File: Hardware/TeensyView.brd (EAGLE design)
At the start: 35.6 x 17.8 mm, 23 parts, among them J1 DNP, J2 DNP

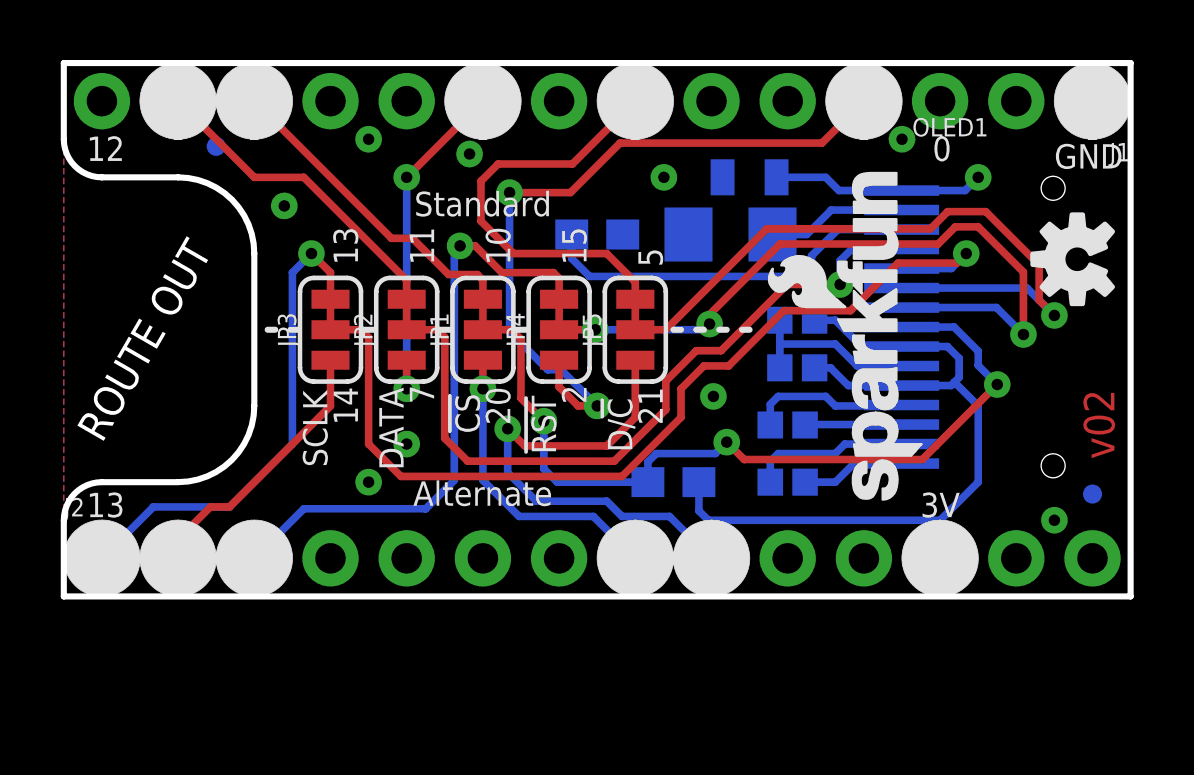
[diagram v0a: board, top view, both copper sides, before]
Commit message: Adjusted proto 2 in prep for reds review
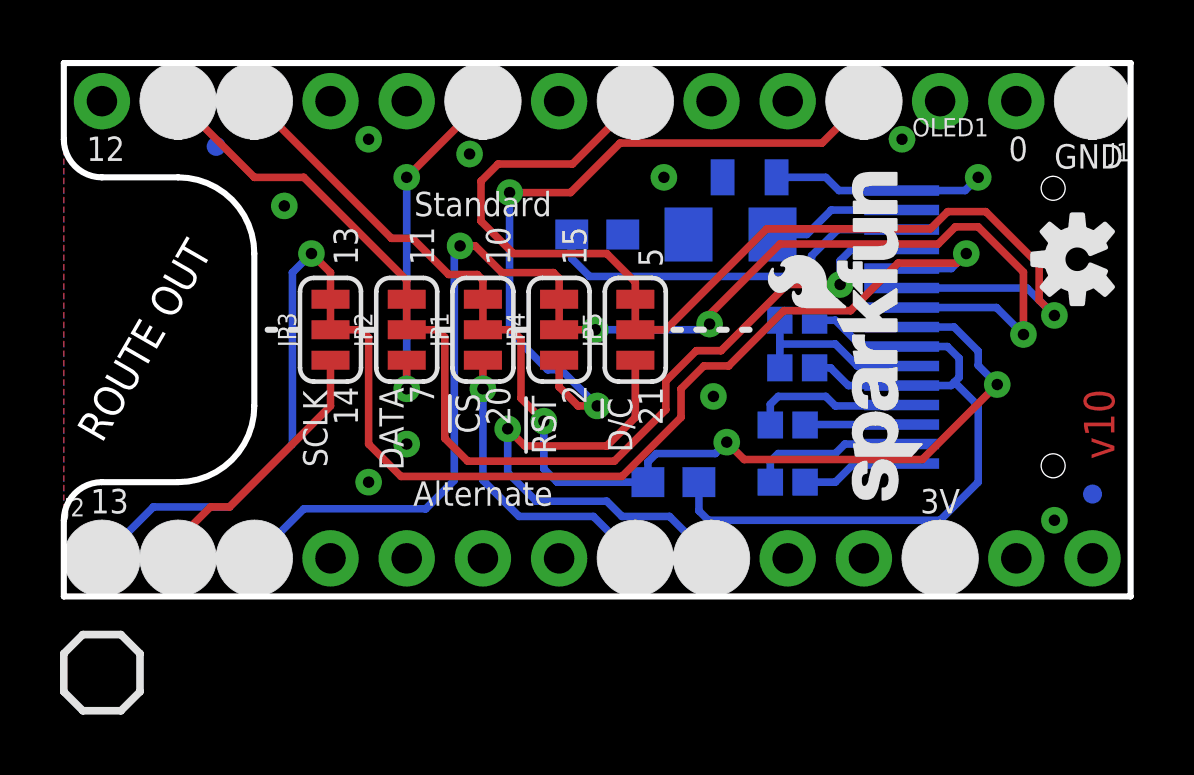
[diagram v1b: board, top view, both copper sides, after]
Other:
- board text added: "v10"
- board text removed: "v02"
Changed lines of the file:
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@@
 <?xml version="1.0" encoding="utf-8"?>
 <!DOCTYPE eagle SYSTEM "eagle.dtd">
-<eagle version="7.5.0">
+<eagle version="7.7.0">
 <drawing>
 <settings>
@@
 <setting verticaltext="up"/>
 </settings>
-<grid distance="0.05" unitdist="inch" unit="inch" style="lines" multiple="1" display="yes" altdistance="0.005" altunitdist="inch" altunit="inch"/>
+<grid distance="0.05" unitdist="inch" unit="inch" style="lines" multiple="1" display="yes" altdistance="0.0025" altunitdist="inch" altunit="inch"/>
 <layers>
-<layer number="1" name="Top" color="4" fill="1" visible="no" active="yes"/>
+<layer number="1" name="Top" color="4" fill="1" visible="yes" active="yes"/>
 <layer number="2" name="Route2" color="1" fill="3" visible="no" active="no"/>
 <layer number="3" name="Route3" color="4" fill="3" visible="no" active="no"/>
@@
 <layer number="19" name="Unrouted" color="6" fill="1" visible="yes" active="yes"/>
 <layer number="20" name="Dimension" color="15" fill="1" visible="yes" active="yes"/>
-<layer number="21" name="tPlace" color="16" fill="1" visible="no" active="yes"/>
+<layer number="21" name="tPlace" color="16" fill="1" visible="yes" active="yes"/>
 <layer number="22" name="bPlace" color="14" fill="1" visible="yes" active="yes"/>
 <layer number="23" name="tOrigins" color="15" fill="1" visible="yes" active="yes"/>
@@
 <layer number="28" name="bValues" color="7" fill="1" visible="no" active="yes"/>
 <layer number="29" name="tStop" color="7" fill="3" visible="no" active="yes"/>
-<layer number="30" name="bStop" color="7" fill="6" visible="no" active="yes"/>
+<layer number="30" name="bStop" color="7" fill="6" visible="yes" active="yes"/>
 <layer number="31" name="tCream" color="7" fill="4" visible="no" active="yes"/>
-<layer number="32" name="bCream" color="7" fill="5" visible="no" active="yes"/>
+<layer number="32" name="bCream" color="7" fill="5" visible="yes" active="yes"/>
 <layer number="33" name="tFinish" color="6" fill="3" visible="no" active="yes"/>
 <layer number="34" name="bFinish" color="6" fill="6" visible="no" active="yes"/>
@@
 <wire x1="1.27" y1="3.81" x2="0" y2="2.54" width="0.2032" layer="20" curve="90"/>
 <wire x1="0" y1="2.54" x2="0" y2="0" width="0.2032" layer="20"/>
-<text x="35.02025" y="4.572" size="1.016" layer="1" font="vector" ratio="25" rot="R90">v02</text>
+<text x="35.02025" y="4.572" size="1.016" layer="1" font="vector" ratio="25" rot="R90">v10</text>
 <text x="17.78" y="-24.13" size="1.778" layer="51" font="vector">Marshall Taylor</text>
 <text x="8.382" y="5.588" size="0.8128" layer="21" font="vector" ratio="15" rot="R90" align="center">SCLK</text>
@@
 </polygon>
 <text x="1.397" y="14.9225" size="0.8128" layer="21" font="vector" ratio="15" rot="R180" align="center">12</text>
-<text x="29.2735" y="14.9225" size="0.8128" layer="21" font="vector" ratio="15" align="center">0</text>
-<text x="1.397" y="3.048" size="0.8128" layer="21" font="vector" ratio="15" rot="R180" align="center">13</text>
+<text x="31.8135" y="14.9225" size="0.8128" layer="21" font="vector" ratio="15" align="center">0</text>
+<text x="1.524" y="3.175" size="0.8128" layer="21" font="vector" ratio="15" rot="R180" align="center">13</text>
 <text x="34.163" y="14.6685" size="0.8128" layer="21" font="vector" ratio="15" rot="R180" align="center">GND</text>
-<text x="29.21" y="3.048" size="0.8128" layer="21" font="vector" ratio="15" rot="R180" align="center">3V</text>
+<text x="29.21" y="3.175" size="0.8128" layer="21" font="vector" ratio="15" rot="R180" align="center">3V</text>
 <wire x1="9.9695" y1="8.89" x2="10.3505" y2="8.89" width="0.2032" layer="21"/>
 <wire x1="12.5095" y1="8.89" x2="12.8905" y2="8.89" width="0.2032" layer="21"/>
@@
 </polygon>
 <text x="1.397" y="14.9225" size="0.8128" layer="22" font="vector" ratio="15" rot="MR180" align="center">12</text>
-<text x="34.7345" y="14.76375" size="0.8128" layer="22" font="vector" ratio="15" rot="MR0" align="center">G</text>
-<text x="1.397" y="3.048" size="0.8128" layer="22" font="vector" ratio="15" rot="MR180" align="center">13</text>
-<text x="30.353" y="2.7305" size="0.8128" layer="22" font="vector" ratio="15" rot="MR180" align="center">3V</text>
+<text x="34.7345" y="14.63675" size="0.8128" layer="22" font="vector" ratio="15" rot="MR0" align="center">G</text>
+<text x="1.524" y="3.175" size="0.8128" layer="22" font="vector" ratio="15" rot="MR180" align="center">13</text>
+<text x="30.353" y="2.794" size="0.8128" layer="22" font="vector" ratio="15" rot="MR180" align="center">3V</text>
 <text x="1.27" y="5.08" size="1.016" layer="20" font="vector" ratio="15" rot="R60">ROUTE OUT</text>
 <text x="30.099" y="13.5255" size="0.8128" layer="22" font="vector" ratio="15" rot="MR0" align="center">15</text>
 <text x="29.6545" y="4.445" size="0.8128" layer="22" font="vector" ratio="15" rot="MR0" align="center">1</text>
+<wire x1="0" y1="-1.905" x2="0.635" y2="-1.27" width="0.254" layer="21"/>
+<wire x1="0.635" y1="-1.27" x2="1.905" y2="-1.27" width="0.254" layer="21"/>
+<wire x1="1.905" y1="-1.27" x2="2.54" y2="-1.905" width="0.254" layer="21"/>
+<wire x1="2.54" y1="-1.905" x2="2.54" y2="-3.175" width="0.254" layer="21"/>
+<wire x1="2.54" y1="-3.175" x2="1.905" y2="-3.81" width="0.254" layer="21"/>
+<wire x1="1.905" y1="-3.81" x2="0.635" y2="-3.81" width="0.254" layer="21"/>
+<wire x1="0.635" y1="-3.81" x2="0" y2="-3.175" width="0.254" layer="21"/>
+<wire x1="0" y1="-3.175" x2="0" y2="-1.905" width="0.254" layer="21"/>
 </plain>
 <attributes>

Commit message: Made silk and version number changes for reds
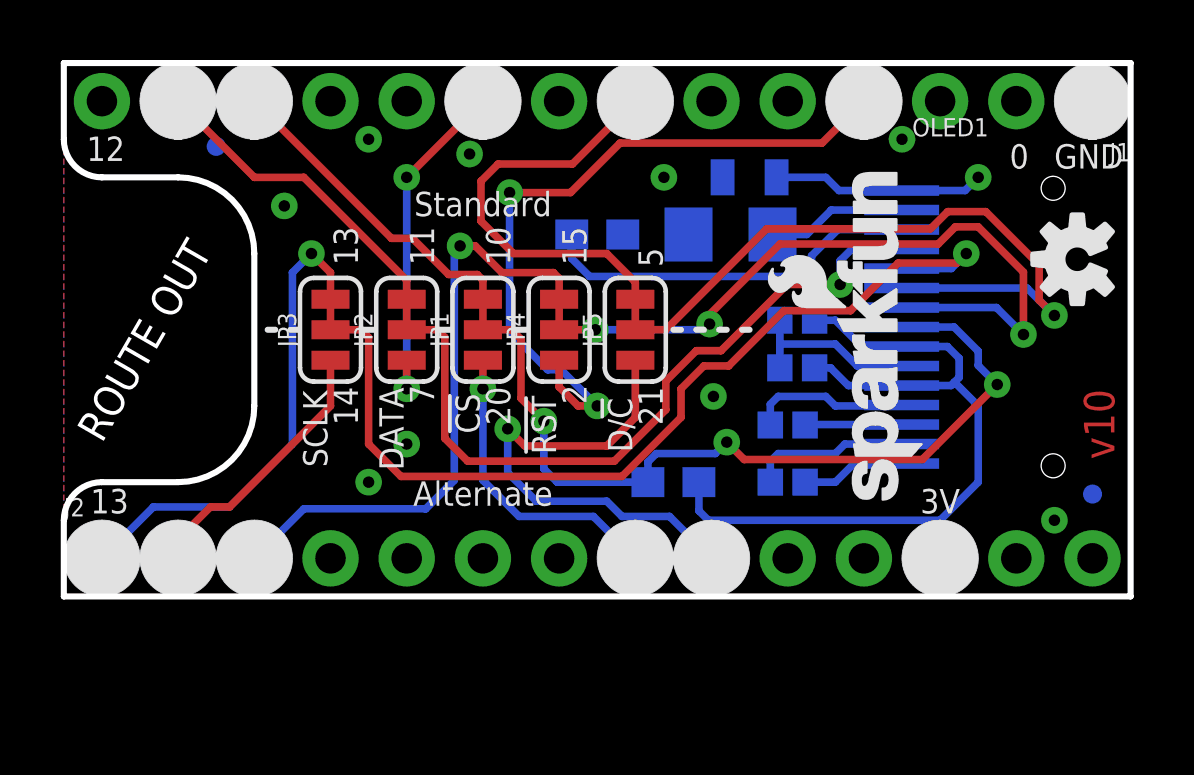
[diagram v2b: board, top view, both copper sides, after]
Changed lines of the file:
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@@
 <setting verticaltext="up"/>
 </settings>
-<grid distance="0.05" unitdist="inch" unit="inch" style="lines" multiple="1" display="yes" altdistance="0.0025" altunitdist="inch" altunit="inch"/>
+<grid distance="0.05" unitdist="inch" unit="inch" style="lines" multiple="1" display="yes" altdistance="0.00125" altunitdist="inch" altunit="inch"/>
 <layers>
 <layer number="1" name="Top" color="4" fill="1" visible="yes" active="yes"/>
@@
 </polygon>
 <text x="1.397" y="14.9225" size="0.8128" layer="21" font="vector" ratio="15" rot="R180" align="center">12</text>
-<text x="31.8135" y="14.9225" size="0.8128" layer="21" font="vector" ratio="15" align="center">0</text>
+<text x="31.84525" y="14.6685" size="0.8128" layer="21" font="vector" ratio="15" align="center">0</text>
 <text x="1.524" y="3.175" size="0.8128" layer="21" font="vector" ratio="15" rot="R180" align="center">13</text>
 <text x="34.163" y="14.6685" size="0.8128" layer="21" font="vector" ratio="15" rot="R180" align="center">GND</text>
@@
 <text x="30.099" y="13.5255" size="0.8128" layer="22" font="vector" ratio="15" rot="MR0" align="center">15</text>
 <text x="29.6545" y="4.445" size="0.8128" layer="22" font="vector" ratio="15" rot="MR0" align="center">1</text>
-<wire x1="0" y1="-1.905" x2="0.635" y2="-1.27" width="0.254" layer="21"/>
-<wire x1="0.635" y1="-1.27" x2="1.905" y2="-1.27" width="0.254" layer="21"/>
-<wire x1="1.905" y1="-1.27" x2="2.54" y2="-1.905" width="0.254" layer="21"/>
-<wire x1="2.54" y1="-1.905" x2="2.54" y2="-3.175" width="0.254" layer="21"/>
-<wire x1="2.54" y1="-3.175" x2="1.905" y2="-3.81" width="0.254" layer="21"/>
-<wire x1="1.905" y1="-3.81" x2="0.635" y2="-3.81" width="0.254" layer="21"/>
-<wire x1="0.635" y1="-3.81" x2="0" y2="-3.175" width="0.254" layer="21"/>
-<wire x1="0" y1="-3.175" x2="0" y2="-1.905" width="0.254" layer="21"/>
 </plain>
 <attributes>
